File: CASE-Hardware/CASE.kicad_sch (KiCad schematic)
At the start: 57 parts, among them J101 B2B-PH-K-S, J102 TVC_X, J103 TVC_Y, J104 USB_C_Receptacle_USB2.0_16P, SW101 SW_Push, SW103 SW_Push, U101 TPS61022, U102 ECMF02-2AMX6, U103 ESP32-S3-WROOM-1U, U104 TPS2116DRL, U105 TPS63000, U106 BMI323, U107 BMP581

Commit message: Added note on mistake in wiring the ECMF02-2AMX6
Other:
- note added: "WARNING: Pin 3 should be connected to GND, pin 4 should be left unconnected"
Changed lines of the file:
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@@
+	)
+	(rectangle
+		(start 57.15 156.21)
+		(end 81.28 189.23)
+		(stroke
+			(width 0.254)
+			(type dash_dot)
+			(color 255 0 0 1)
+		)
+		(fill
+			(type none)
+		)
 	)
 	(rectangle
@@
 		)
 	)
+	(text "WARNING: Pin 3 should \nbe connected to GND, \npin 4 should be left \nunconnected"
+		(exclude_from_sim no)
+		(at 57.912 184.658 0)
+		(effects
+			(font
+				(size 1.27 1.27)
+				(color 255 0 0 1)
+			)
+			(justify left)
+		)
+	)

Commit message: Added reference schematics for voltage regulators from Power Designer
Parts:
- added U108: ECMF02-2AMX6, Package_DFN_QFN:ST_UQFN-6L_1.5x1.7mm_P0.5mm, symbol Power_Protection:ECMF02-2AMX6
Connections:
- net GND: now also U108.3 (GND), U108.4 (NC)
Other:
- note added: "CORRECT CONFIGURATION"
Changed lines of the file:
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@@
 	)
 	(rectangle
+		(start 54.61 203.2)
+		(end 83.82 234.95)
+		(stroke
+			(width 0.254)
+			(type dash_dot)
+			(color 0 132 0 1)
+		)
+		(fill
+			(type none)
+		)
+	)
+	(rectangle
 		(start 124.46 15.24)
 		(end 171.45 33.02)
@@
 		)
 	)
+	(text "CORRECT CONFIGURATION"
+		(exclude_from_sim no)
+		(at 57.404 232.918 0)
+		(effects
+			(font
+				(size 1.27 1.27)
+				(color 0 132 0 1)
+			)
+			(justify left)
+		)
+	)
 	(text "MCU Boot Delay"
 		(exclude_from_sim no)
@@
 	)
 	(junction
+		(at 71.12 224.79)
+		(diameter 0)
+		(color 0 0 0 0)
+	)
+	(junction
 		(at 231.14 156.21)
 		(diameter 0)
@@
 	(wire
 		(pts
+			(xy 68.58 224.79) (xy 71.12 224.79)
+		)
+		(stroke
+			(width 0)
+			(type default)
+		)
+	)
+	(wire
+		(pts
 			(xy 256.54 86.36) (xy 262.89 86.36)
 		)
@@
 	(wire
 		(pts
+			(xy 68.58 222.25) (xy 68.58 224.79)
+		)
+		(stroke
+			(width 0)
+			(type default)
+		)
+	)
+	(wire
+		(pts
 			(xy 215.9 138.43) (xy 215.9 139.7)
 		)
@@
 	(wire
 		(pts
+			(xy 71.12 222.25) (xy 71.12 224.79)
+		)
+		(stroke
+			(width 0)
+			(type default)
+		)
+	)
+	(wire
+		(pts
 			(xy 256.54 107.95) (xy 262.89 107.95)
 		)
@@
 	(wire
 		(pts
+			(xy 71.12 224.79) (xy 71.12 227.33)
+		)
+		(stroke
+			(width 0)
+			(type default)
+		)
+	)
+	(wire
+		(pts
 			(xy 55.88 64.77) (xy 59.69 64.77)
 		)
@@
 	)
 	(symbol
+		(lib_id "Power_Protection:ECMF02-2AMX6")
+		(at 68.58 214.63 0)
+		(unit 1)
+		(exclude_from_sim no)
+		(in_bom yes)
+		(on_board yes)
+		(dnp no)
+		(property "Reference" "U108"
+			(at 68.58 206.502 0)
+			(effects
+				(font
+					(size 1.27 1.27)
+				)
+			)
+		)
+		(property "Value" "ECMF02-2AMX6"
+			(at 68.58 208.28 0)
+			(effects
+				(font
+					(size 1.27 1.27)
+				)
+			)
+		)
+		(property "Footprint" "Package_DFN_QFN:ST_UQFN-6L_1.5x1.7mm_P0.5mm"
+			(at 68.58 234.95 0)
+			(effects
+				(font
+					(size 1.27 1.27)
+				)
+				(hide yes)
+			)
+		)
+		(property "Datasheet" "https://www.st.com/resource/en/datasheet/ecmf02-2amx6.pdf"
+			(at 68.58 237.49 0)
+			(effects
+				(font
+					(size 1.27 1.27)
+				)
+				(hide yes)
+			)
+		)
+		(property "Description" "Single Pair Common Mode Filter with ESD Protection, UQFN-6L"
+			(at 68.58 214.63 0)
+			(effects
+				(font
+					(size 1.27 1.27)
+				)
+				(hide yes)
+			)
+		)
+		(pin "2"
+		)
+		(pin "1"
+		)
+		(pin "3"
+		)
+		(pin "4"
+		)
+		(pin "6"
+		)
+		(pin "5"
+		)
+		(instances
+			(project "CASE"
+				(path "/be8da508-0732-4f37-93ed-c5b606d31b4d"
+					(reference "U108")
+					(unit 1)
+				)
+			)
+		)
+	)
+	(symbol
 		(lib_id "power:+3V3")
 		(at 171.45 52.07 0)
@@
 					(unit 1)
 				)
+			)
+		)
+	)
+	(symbol
+		(lib_id "power:GND")
+		(at 71.12 227.33 0)
+		(unit 1)
+		(exclude_from_sim no)
+		(in_bom yes)
+		(on_board yes)
+		(dnp no)
+		(property "Reference" "#PWR0137"
+			(at 71.12 233.68 0)
+			(effects
+				(font
+					(size 1.27 1.27)
+				)
+				(hide yes)
+			)
+		)
+		(property "Value" "GND"
+			(at 75.184 229.362 0)
+			(effects
+				(font
+					(size 1.27 1.27)
+				)
+			)
+		)
+		(property "Footprint" ""
+			(at 71.12 227.33 0)
+			(effects
+				(font
+					(size 1.27 1.27)
+				)
+				(hide yes)
+			)
+		)
+		(property "Datasheet" ""
+			(at 71.12 227.33 0)
+			(effects
+				(font
+					(size 1.27 1.27)
+				)
+				(hide yes)
+			)
+		)
+		(property "Description" "Power symbol creates a global label with name \"GND\" , ground"
+			(at 71.12 227.33 0)
+			(effects
+				(font
+					(size 1.27 1.27)
+				)
+				(hide yes)
+			)
+		)
+		(pin "1"
+		)
+		(instances
+			(project "CASE"
+				(path "/be8da508-0732-4f37-93ed-c5b606d31b4d"
+					(reference "#PWR0137")
+					(unit 1)
+				)

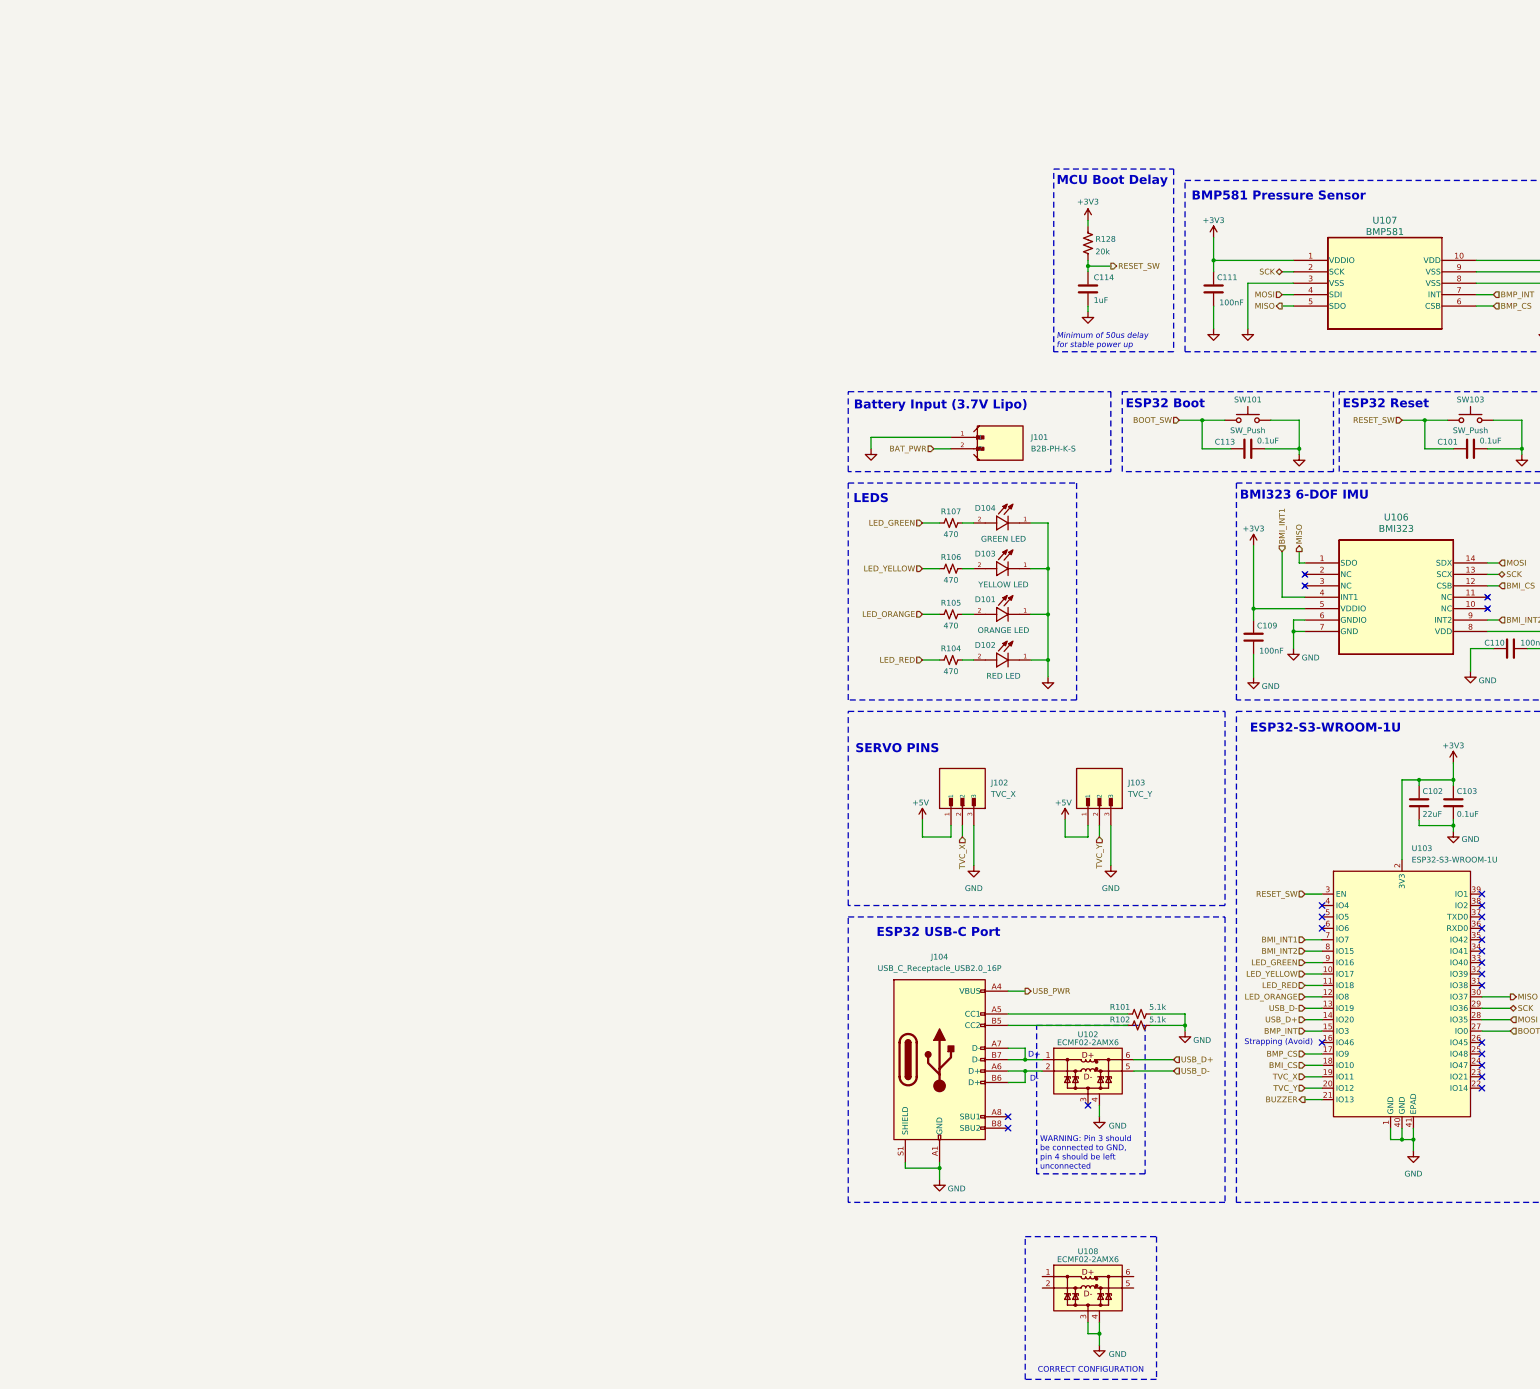
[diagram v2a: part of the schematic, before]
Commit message: Added notes to mistakes in schematic
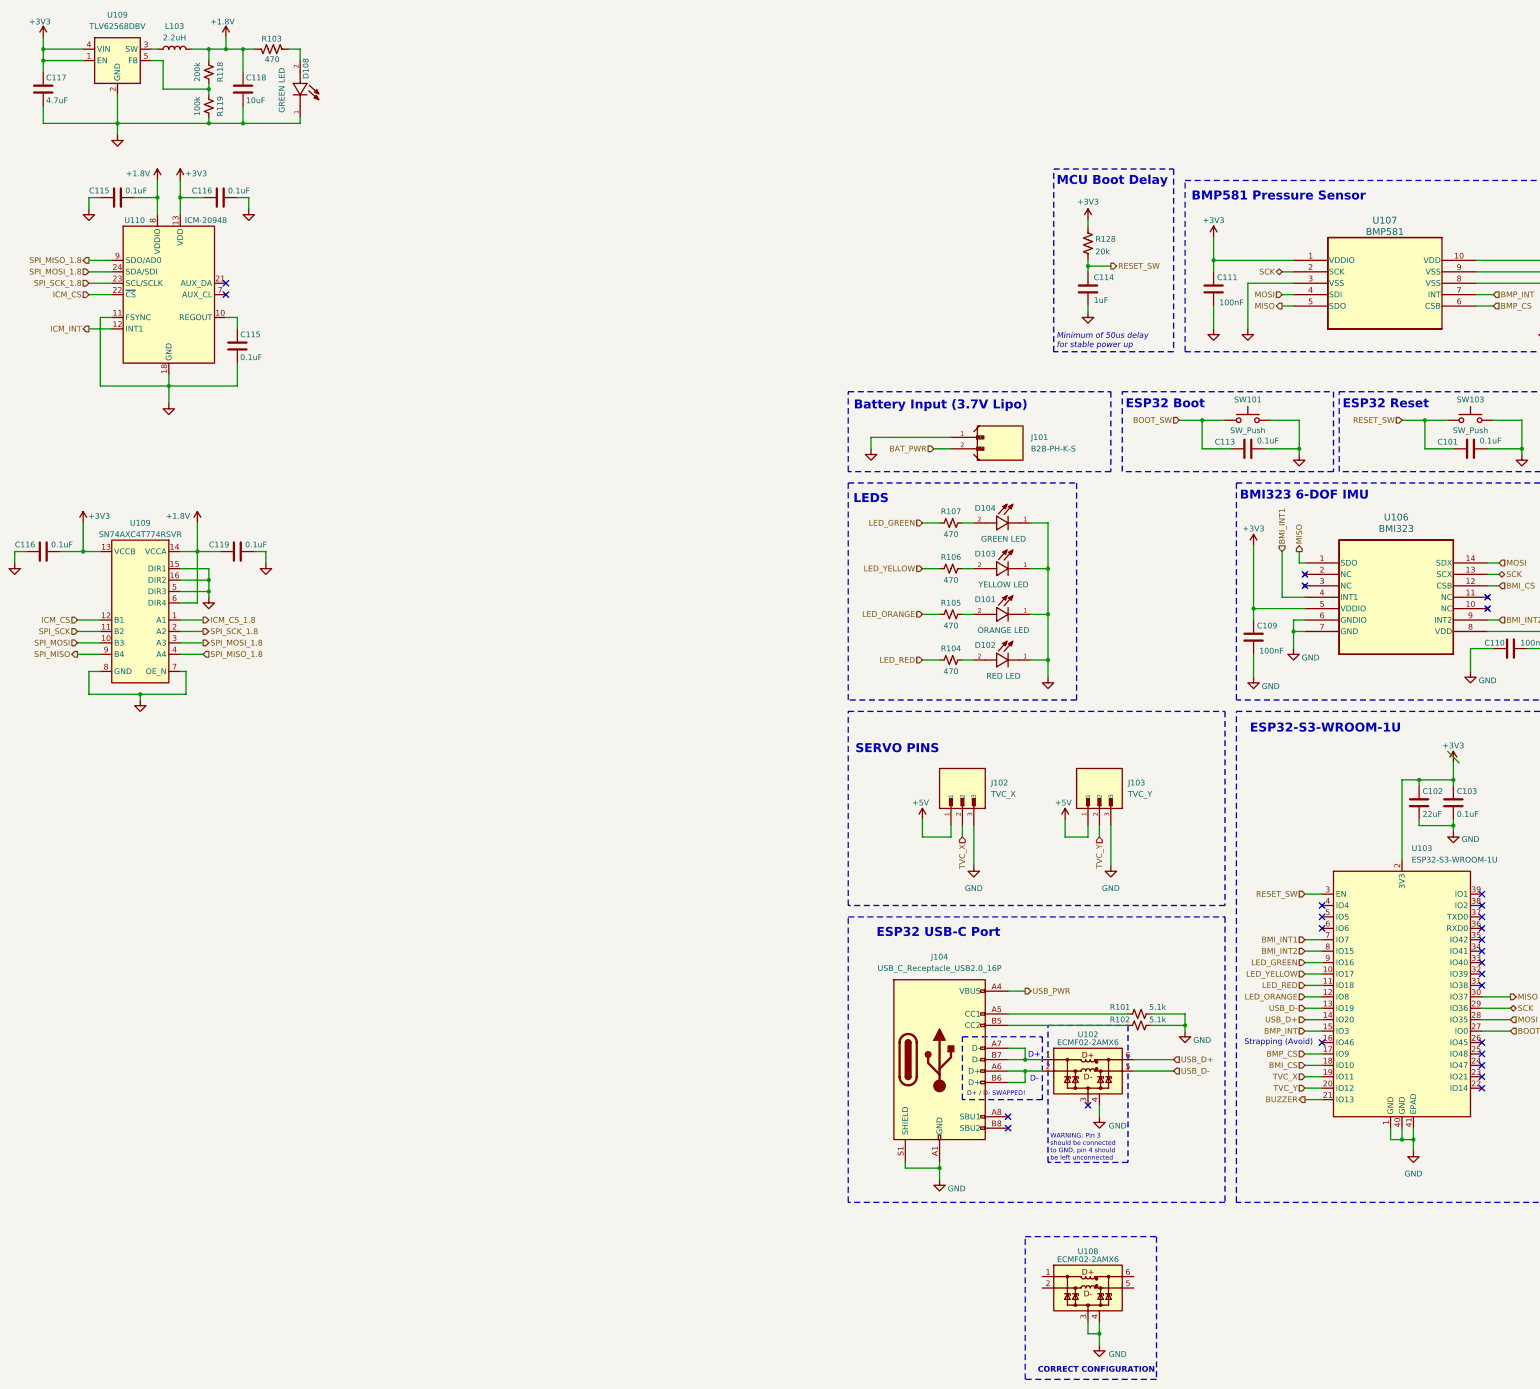
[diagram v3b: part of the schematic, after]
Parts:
- added C115 (x2), C116 (x2), C119: 0.1uF, Capacitor_SMD:C_0805_2012Metric, symbol Device:C
- added C117: 4.7uF, Capacitor_SMD:C_0805_2012Metric, symbol Device:C
- added C118: 10uF, Capacitor_SMD:C_0805_2012Metric, symbol Device:C
- added D108: GREEN LED, APT1608SECK:LED_APT1608SECK, symbol APT1608SECK:APT1608SECK
- added L103: 2.2uH, SDR0403-2R2ML:IND_SDR0403-2R2ML, symbol Device:L
- added R103: 470, Resistor_SMD:R_0805_2012Metric, symbol Device:R_US
- added R118: 200k, Resistor_SMD:R_0805_2012Metric, symbol Device:R_Small_US
- added R119: 100k, Resistor_SMD:R_0805_2012Metric, symbol Device:R_Small_US
- added U109: TLV62568DBV, Package_TO_SOT_SMD:SOT-23-5, symbol Regulator_Switching:TLV62568DBV
- added U109: SN74AXC4T774RSVR, SN74AXC4T774RSVR:QFN40P260X180X55-16N, symbol 74xGxx:_SN74AXC4T774RSVR
- added U110: ICM-20948, Sensor_Motion:InvenSense_QFN-24_3x3mm_P0.4mm, symbol Sensor_Motion:ICM-20948
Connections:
- net +3V3: now also C116.1, C116.2, C117.1, U109.1 (EN), U109.13 (VCCB), U109.4 (VIN), U110.13 (VDD)
- net GND: now also C115.1, C115.2, C116.1, C116.2, C117.2, C118.2, C119.2, D108.1, R119.2, U109.15 (DIR1), U109.16 (DIR2), U109.2 (GND), U109.5 (DIR3), U109.7 (OE_N), U109.8 (GND), U110.11 (FSYNC), U110.18 (GND), U110.20 (GND)
- new net: L103.1, U109.3 (SW)
- new net: R118.2, R119.1, U109.5 (FB)
- new net: D108.2, R103.2
- new net: C115.1, U110.10 (REGOUT)
- new net +1.8V: C115.2, C118.1, C119.1, L103.2, R103.1, R118.1, U109.14 (VCCA), U109.6 (DIR4), U110.8 (VDDIO)
- new net ICM_CS: U109.12 (B1), U110.22 (~{CS})
- new net ICM_CS_1.8: U109.1 (A1)
- new net ICM_INT: U110.12 (INT1)
- new net SPI_MISO: U109.9 (B4)
- new net SPI_MISO_1.8: U109.4 (A4), U110.9 (SDO/AD0)
- new net SPI_MOSI: U109.10 (B3)
- new net SPI_MOSI_1.8: U109.3 (A3), U110.24 (SDA/SDI)
- new net SPI_SCK: U109.11 (B2)
- new net SPI_SCK_1.8: U109.2 (A2), U110.23 (SCL/SCLK)
- no-connect marks 26 -> 28
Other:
- note added: "D+ / D- SWAPPED!"
